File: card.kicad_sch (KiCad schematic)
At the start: 10 parts, among them U1 ISP1907, U2 MTCH6102

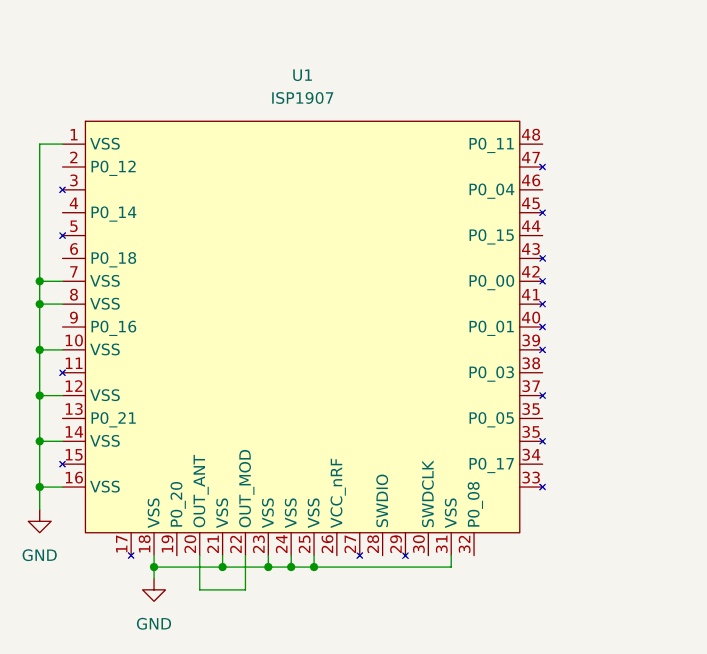
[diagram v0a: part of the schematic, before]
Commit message: update isp1907 symbol
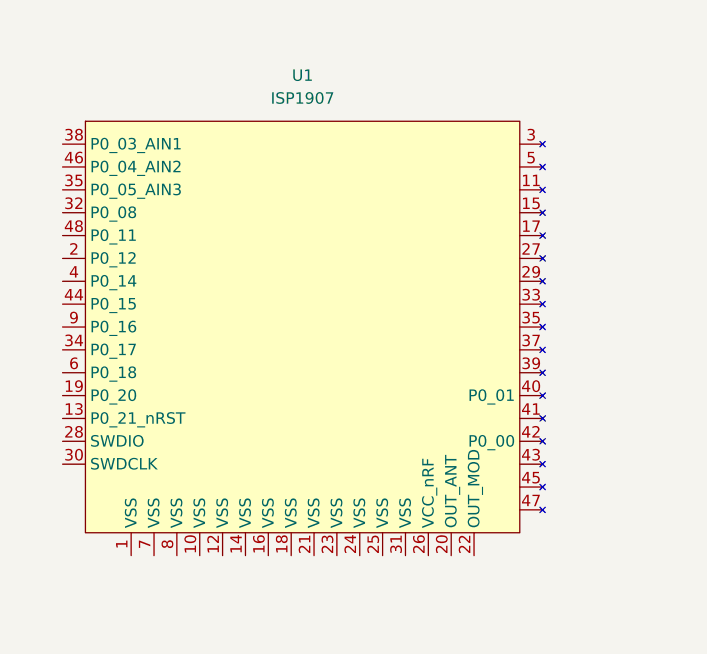
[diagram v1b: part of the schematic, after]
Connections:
- net GND: no longer U1.1 (VSS), U1.10 (VSS), U1.12 (VSS), U1.14 (VSS), U1.16 (VSS), U1.18 (VSS), U1.21 (VSS), U1.23 (VSS), U1.24 (VSS), U1.25 (VSS), U1.31 (VSS), U1.7 (VSS), U1.8 (VSS)
- net at U1.20 (OUT_ANT): no longer U1.22 (OUT_MOD)

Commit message: update
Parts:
- added R5: 10k, symbol Device:R
- added SW1: SW_Push, symbol Switch:SW_Push
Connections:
- net +BATT: now also U1.26 (VCC_nRF), R5.1
- net GND: now also U1.1 (VSS), U1.10 (VSS), U1.12 (VSS), U1.14 (VSS), U1.16 (VSS), U1.18 (VSS), U1.21 (VSS), U1.23 (VSS), U1.24 (VSS), U1.25 (VSS), U1.31 (VSS), U1.7 (VSS), U1.8 (VSS), SW1.1
- net RESET: now reaches U1.13 (P0_21_nRST)
- net RESET: now also R5.2, SW1.2
- net at U1.20 (OUT_ANT): now also U1.22 (OUT_MOD)
- net SWDIO: now reaches U1.28 (SWDIO)
- net SWDCLK: now reaches U1.30 (SWDCLK)

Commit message: basic schematic
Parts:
- removed SW1: SW_Push, symbol Switch:SW_Push
- R5: value 10k -> 20k
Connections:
- net SYNC: now reaches R4.2, U2.12 (SYNC)
- net SDA: now reaches R2.2, U2.15 (SDA)
- net at U2.1 (NRST): now also R5.2
- net INT: now reaches R3.2, U2.11 (INT)
- net SCL: now reaches R1.2, U2.14 (SCL)
- net RESET: no longer names the net of U1.13 (P0_21_nRST)
- net RESET: no longer R5.2

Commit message: basic pcb layout
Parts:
- C1, C2: footprint (none) -> Capacitor_SMD:C_0402_1005Metric
- D1: footprint (none) -> Diode_SMD:D_SMA
- R1, R2, R3, R4, R5: footprint (none) -> Resistor_SMD:R_0603_1608Metric
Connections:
- net SCL: now also U1.6 (P0_18)
- net SDA: now also U1.19 (P0_20)
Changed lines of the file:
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@@
+	(wire
+		(pts
+			(xy 40.64 66.04) (xy 50.8 66.04)
+		)
+		(stroke
+			(width 0)
+			(type default)
+		)
+	)
 	(wire
 		(pts
@@
 		(pts
 			(xy 163.83 33.02) (xy 170.18 33.02)
+		)
+		(stroke
+			(width 0)
+			(type default)
+		)
+	)
+	(wire
+		(pts
+			(xy 40.64 68.58) (xy 50.8 68.58)
 		)
 		(stroke
@@
 		)
 	)
-	(label "SCL"
-		(at 172.72 43.18 0)
+	(label "SDA"
+		(at 40.64 68.58 0)
 		(fields_autoplaced yes)
 		(effects
@@
 		)
 	)
+	(label "SCL"
+		(at 172.72 43.18 0)
+		(fields_autoplaced yes)
+		(effects
+			(font
+				(size 1.27 1.27)
+			)
+			(justify left bottom)
+		)
+	)
 	(label "SYNC"
 		(at 172.72 50.8 0)
+		(fields_autoplaced yes)
+		(effects
+			(font
+				(size 1.27 1.27)
+			)
+			(justify left bottom)
+		)
+	)
+	(label "SCL"
+		(at 40.64 66.04 0)
 		(fields_autoplaced yes)
 		(effects
@@
 			)
 		)
-		(property "Footprint" ""
+		(property "Footprint" "Diode_SMD:D_SMA"
 			(at 254 41.91 0)
 			(effects
@@
 			)
 		)
-		(property "Footprint" ""
+		(property "Footprint" "Resistor_SMD:R_0603_1608Metric"
 			(at 149.352 36.83 90)
 			(effects
@@
 			)
 		)
-		(property "Footprint" ""
+		(property "Footprint" "Resistor_SMD:R_0603_1608Metric"
 			(at 162.052 36.83 90)
 			(effects
@@
 			)
 		)
-		(property "Footprint" ""
+		(property "Footprint" "Capacitor_SMD:C_0402_1005Metric"
 			(at 222.25 58.42 0)
 			(effects
@@
 			)
 		)
-		(property "Footprint" ""
+		(property "Footprint" "Capacitor_SMD:C_0402_1005Metric"
 			(at 215.9 58.42 0)
 			(effects
@@
 			)
 		)
-		(property "Footprint" ""
+		(property "Footprint" "Resistor_SMD:R_0603_1608Metric"
 			(at 155.702 36.83 90)
 			(effects
@@
 			)
 		)
-		(property "Footprint" ""
+		(property "Footprint" "Resistor_SMD:R_0603_1608Metric"
 			(at 168.402 36.83 90)
 			(effects
@@
 			)
 		)
-		(property "Footprint" ""
+		(property "Footprint" "Resistor_SMD:R_0603_1608Metric"
 			(at 177.292 36.83 90)
 			(effects

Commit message: 80%
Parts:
- added C3: 100u, Capacitor_SMD:C_1206_3216Metric, symbol Device:C
- added D2: LED, LED_SMD:LED_0603_1608Metric, symbol Device:LED
- added J1: Conn_01x08, Connector_PinHeader_2.54mm:PinHeader_1x08_P2.54mm_Vertical, symbol Connector_Generic:Conn_01x08
- added J2: Conn_01x04, Connector_PinHeader_2.54mm:PinHeader_1x04_P2.54mm_Vertical, symbol Connector_Generic:Conn_01x04
- added R6: 2.2k, Resistor_SMD:R_0603_1608Metric, symbol Device:R
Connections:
- net +BATT: now also C3.1, J2.4 (Pin_4)
- net GND: now also C3.2, J2.2 (Pin_2), R6.2
- net INT: now also U1.6 (P0_18)
- net SCL: now also U1.2 (P0_12); no longer U1.6 (P0_18)
- net SDA: now also U1.9 (P0_16); no longer U1.19 (P0_20)
- net SWDCLK: now also J2.1 (Pin_1)
- net SWDIO: now also J2.3 (Pin_3)
- net SYNC: now also U1.4 (P0_14)
- net ~{RESET}: now reaches U1.13 (P0_21_nRST)
- net ~{RESET}: now also J1.1 (Pin_1)
- net P0_08: now reaches U1.32 (P0_08)
- net P0_08: now also J1.2 (Pin_2)
- net P0_17: now reaches U1.34 (P0_17)
- net P0_17: now also J1.3 (Pin_3)
- net P0_03: now reaches U1.38 (P0_03_AIN1)
- net P0_03: now also J1.5 (Pin_5)
- net P0_15: now reaches U1.44 (P0_15)
- net P0_15: now also J1.6 (Pin_6)
- net P0_04: now reaches U1.46 (P0_04_AIN2)
- net P0_04: now also J1.7 (Pin_7)
- net P0_11: now reaches U1.48 (P0_11)
- net P0_11: now also J1.8 (Pin_8)
- new net: D2.2 (A), U1.19 (P0_20)
- new net: D2.1 (K), R6.1
- new net P0_05: J1.4 (Pin_4), U1.36 (P0_05_AIN3)
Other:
- moved on the sheet: U1

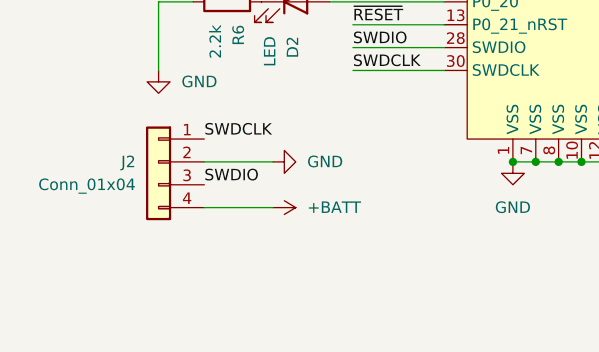
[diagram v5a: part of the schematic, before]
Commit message: add qwiic conn and fillet traces
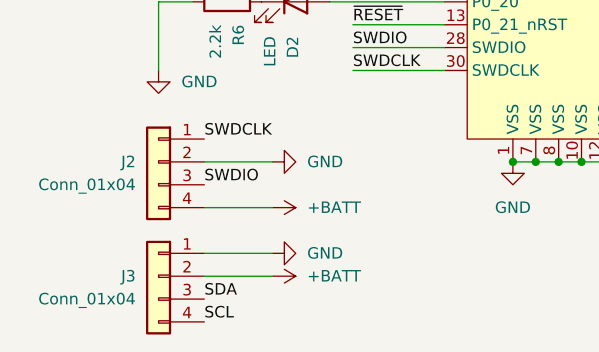
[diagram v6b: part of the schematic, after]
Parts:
- added J3: Conn_01x04, Connector_JST:JST_SH_SM04B-SRSS-TB_1x04-1MP_P1.00mm_Horizontal, symbol Connector_Generic:Conn_01x04
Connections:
- net +BATT: now also J3.2 (Pin_2)
- net GND: now also J3.1 (Pin_1)
- net SCL: now also J3.4 (Pin_4)
- net SDA: now also J3.3 (Pin_3)
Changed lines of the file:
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@@
+	(wire
+		(pts
+			(xy 36.83 99.06) (xy 44.45 99.06)
+		)
+		(stroke
+			(width 0)
+			(type default)
+		)
+	)
 	(wire
 		(pts
@@
 		(pts
 			(xy 96.52 86.36) (xy 99.06 86.36)
+		)
+		(stroke
+			(width 0)
+			(type default)
+		)
+	)
+	(wire
+		(pts
+			(xy 36.83 96.52) (xy 44.45 96.52)
 		)
 		(stroke
@@
 		)
 	)
+	(label "SDA"
+		(at 36.83 101.6 0)
+		(fields_autoplaced yes)
+		(effects
+			(font
+				(size 1.27 1.27)
+			)
+			(justify left bottom)
+		)
+	)
 	(label "P0_15"
 		(at 36.83 53.34 0)
@@
 	(label "P0_04"
 		(at 53.34 43.18 0)
+		(fields_autoplaced yes)
+		(effects
+			(font
+				(size 1.27 1.27)
+			)
+			(justify left bottom)
+		)
+	)
+	(label "SCL"
+		(at 36.83 104.14 0)
 		(fields_autoplaced yes)
 		(effects
@@
 	)
 	(symbol
+		(lib_id "Connector_Generic:Conn_01x04")
+		(at 31.75 99.06 0)
+		(mirror y)
+		(unit 1)
+		(exclude_from_sim no)
+		(in_bom yes)
+		(on_board yes)
+		(dnp no)
+		(fields_autoplaced yes)
+		(property "Reference" "J3"
+			(at 29.21 99.0599 0)
+			(effects
+				(font
+					(size 1.27 1.27)
+				)
+				(justify left)
+			)
+		)
+		(property "Value" "Conn_01x04"
+			(at 29.21 101.5999 0)
+			(effects
+				(font
+					(size 1.27 1.27)
+				)
+				(justify left)
+			)
+		)
+		(property "Footprint" "Connector_JST:JST_SH_SM04B-SRSS-TB_1x04-1MP_P1.00mm_Horizontal"
+			(at 31.75 99.06 0)
+			(effects
+				(font
+					(size 1.27 1.27)
+				)
+				(hide yes)
+			)
+		)
+		(property "Datasheet" "~"
+			(at 31.75 99.06 0)
+			(effects
+				(font
+					(size 1.27 1.27)
+				)
+				(hide yes)
+			)
+		)
+		(property "Description" "Generic connector, single row, 01x04, script generated (kicad-library-utils/schlib/autogen/connector/)"
+			(at 31.75 99.06 0)
+			(effects
+				(font
+					(size 1.27 1.27)
+				)
+				(hide yes)
+			)
+		)
+		(pin "1"
+		)
+		(pin "3"
+		)
+		(pin "2"
+		)
+		(pin "4"
+		)
+		(instances
+			(project ""
+				(path "/702c4184-d498-4362-ae32-d42c7ce9136a"
+					(reference "J3")
+					(unit 1)
+				)
+			)
+		)
+	)
+	(symbol
 		(lib_id "power:GND")
 		(at 44.45 86.36 90)
@@
 	)
 	(symbol
+		(lib_id "power:GND")
+		(at 44.45 96.52 90)
+		(unit 1)
+		(exclude_from_sim no)
+		(in_bom yes)
+		(on_board yes)
+		(dnp no)
+		(fields_autoplaced yes)
+		(property "Reference" "#PWR011"
+			(at 50.8 96.52 0)
+			(effects
+				(font
+					(size 1.27 1.27)
+				)
+				(hide yes)
+			)
+		)
+		(property "Value" "GND"
+			(at 48.26 96.5199 90)
+			(effects
+				(font
+					(size 1.27 1.27)
+				)
+				(justify right)
+			)
+		)
+		(property "Footprint" ""
+			(at 44.45 96.52 0)
+			(effects
+				(font
+					(size 1.27 1.27)
+				)
+				(hide yes)
+			)
+		)
+		(property "Datasheet" ""
+			(at 44.45 96.52 0)
+			(effects
+				(font
+					(size 1.27 1.27)
+				)
+				(hide yes)
+			)
+		)
+		(property "Description" "Power symbol creates a global label with name \"GND\" , ground"
+			(at 44.45 96.52 0)
+			(effects
+				(font
+					(size 1.27 1.27)
+				)
+				(hide yes)
+			)
+		)
+		(pin "1"
+		)
+		(instances
+			(project ""
+				(path "/702c4184-d498-4362-ae32-d42c7ce9136a"
+					(reference "#PWR011")
+					(unit 1)
+				)
+			)
+		)
+	)
+	(symbol
 		(lib_id "power:+BATT")
 		(at 44.45 91.44 270)
@@
 					(unit 1)
 				)
+			)
+		)
+	)
+	(symbol
+		(lib_id "power:+BATT")
+		(at 44.45 99.06 270)
+		(unit 1)
+		(exclude_from_sim no)
+		(in_bom yes)
+		(on_board yes)
+		(dnp no)
+		(fields_autoplaced yes)
+		(property "Reference" "#PWR012"
+			(at 40.64 99.06 0)
+			(effects
+				(font
+					(size 1.27 1.27)
+				)
+				(hide yes)
+			)
+		)
+		(property "Value" "+BATT"
+			(at 48.26 99.0599 90)
+			(effects
+				(font
+					(size 1.27 1.27)
+				)
+				(justify left)
+			)
+		)
+		(property "Footprint" ""
+			(at 44.45 99.06 0)
+			(effects
+				(font
+					(size 1.27 1.27)
+				)
+				(hide yes)
+			)
+		)
+		(property "Datasheet" ""
+			(at 44.45 99.06 0)
+			(effects
+				(font
+					(size 1.27 1.27)
+				)
+				(hide yes)
+			)
+		)
+		(property "Description" "Power symbol creates a global label with name \"+BATT\""
+			(at 44.45 99.06 0)
+			(effects
+				(font
+					(size 1.27 1.27)
+				)
+				(hide yes)
+			)
+		)
+		(pin "1"
+		)
+		(instances
+			(project ""
+				(path "/702c4184-d498-4362-ae32-d42c7ce9136a"
+					(reference "#PWR012")
+					(unit 1)
+				)

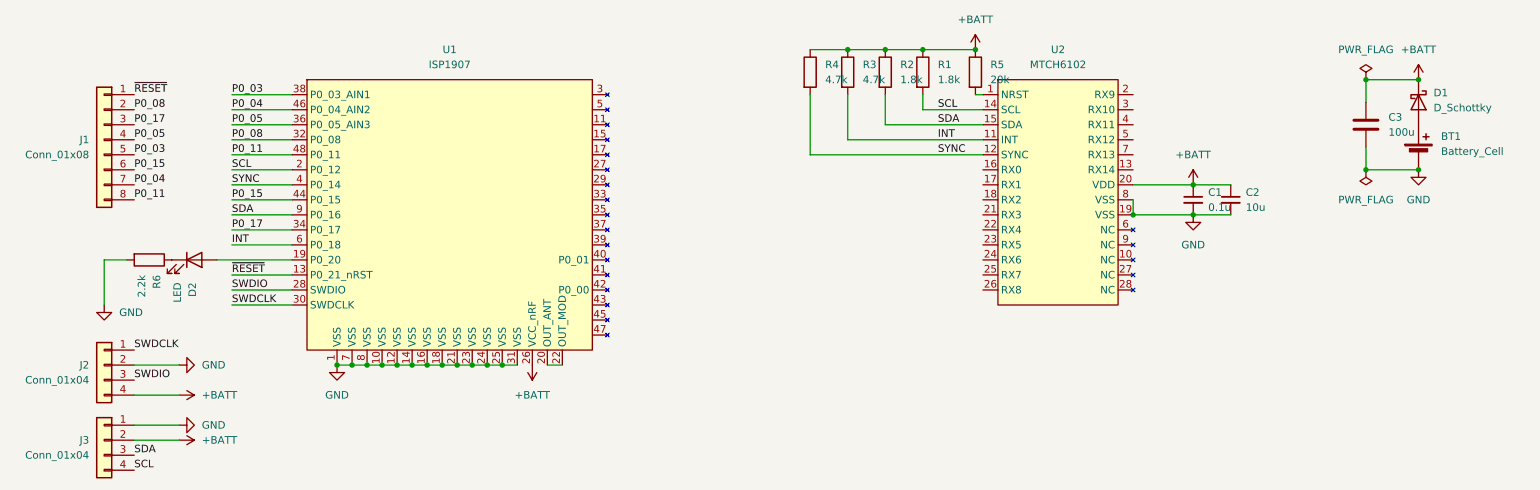
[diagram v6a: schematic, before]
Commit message: add switch
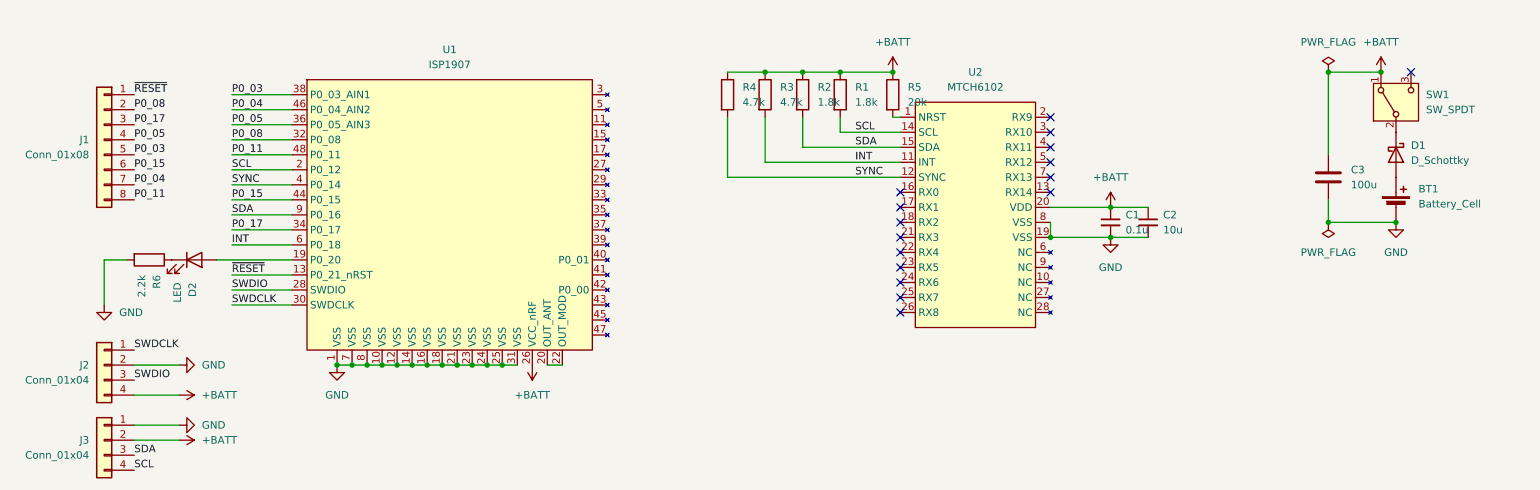
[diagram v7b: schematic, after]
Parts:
- added SW1: SW_SPDT, Button_Switch_SMD:SW_SPDT_PCM12, symbol Switch:SW_SPDT
- D1: footprint Diode_SMD:D_SMA -> Diode_SMD:D_SOD-123
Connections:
- net +BATT: now also SW1.1 (A); no longer D1.1 (K)
- new net: D1.1 (K), SW1.2 (B)
- no-connect marks 0 -> 16
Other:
- moved on the sheet: BT1, C1, C2, C3, D1, R1, R2, R3, R4, R5, U2
